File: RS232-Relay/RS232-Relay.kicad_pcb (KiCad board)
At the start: 2 copper layers, 82.5 x 151 mm, 133 parts, among them J10 Relay 1-4, J11 Relay 1-4, J2 Conn_01x02, J4 Conn_01x09, J5 Conn_01x09, J7 RS232_1, J8 RS232_2, J9 Relay 1-4, K1 G5V-1, K13 G5V-1, K14 G5V-1, K15 G5V-1, K2 G5V-1, K3 G5V-1, K4 G5V-1, K5 G5V-1, K6 G5V-1, K7 G5V-1, K8 G5V-1, K9 G5V-1, Q1 2N3904, Q13 2N3904, Q14 2N3904, Q15 2N3904, Q2 2N3904, Q3 2N3904, Q4 2N3904, Q5 2N3904, Q6 2N3904, Q7 2N3904, Q8 2N3904, Q9 2N3904, SW2 SW_SPST, SW3 SW_SPST, U1 TEC2-1210WI, U2 LTV-847S, U3 PCF8575DBR, U4 MAX3232, U5 LTV-847S, U6 LTV-847S

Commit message: Port labels
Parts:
- added G***: LOGO, LOGO, F.Cu at (142.4, 110.6)
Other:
- board text added: "01"
- board text added: "02"
- board text added: "03"
- board text added: "04"
- board text added: "05"
- board text added: "06"
- board text added: "07"
- board text added: "08"
- board text added: "09"
- board text added: "0V"
- board text added: "10"
- board text added: "11"
- board text added: "12"
- board text added: "12V"

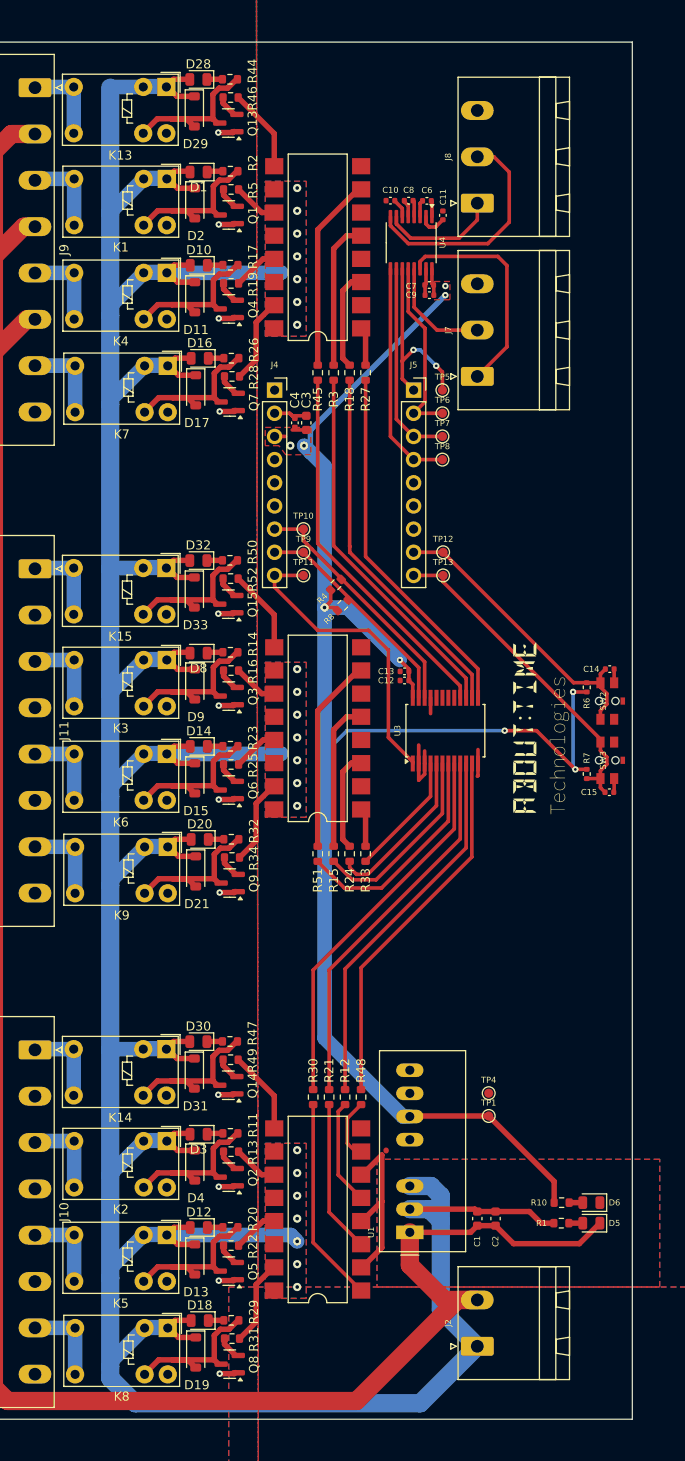
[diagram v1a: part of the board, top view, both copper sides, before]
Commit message: Hide silkscreen designators
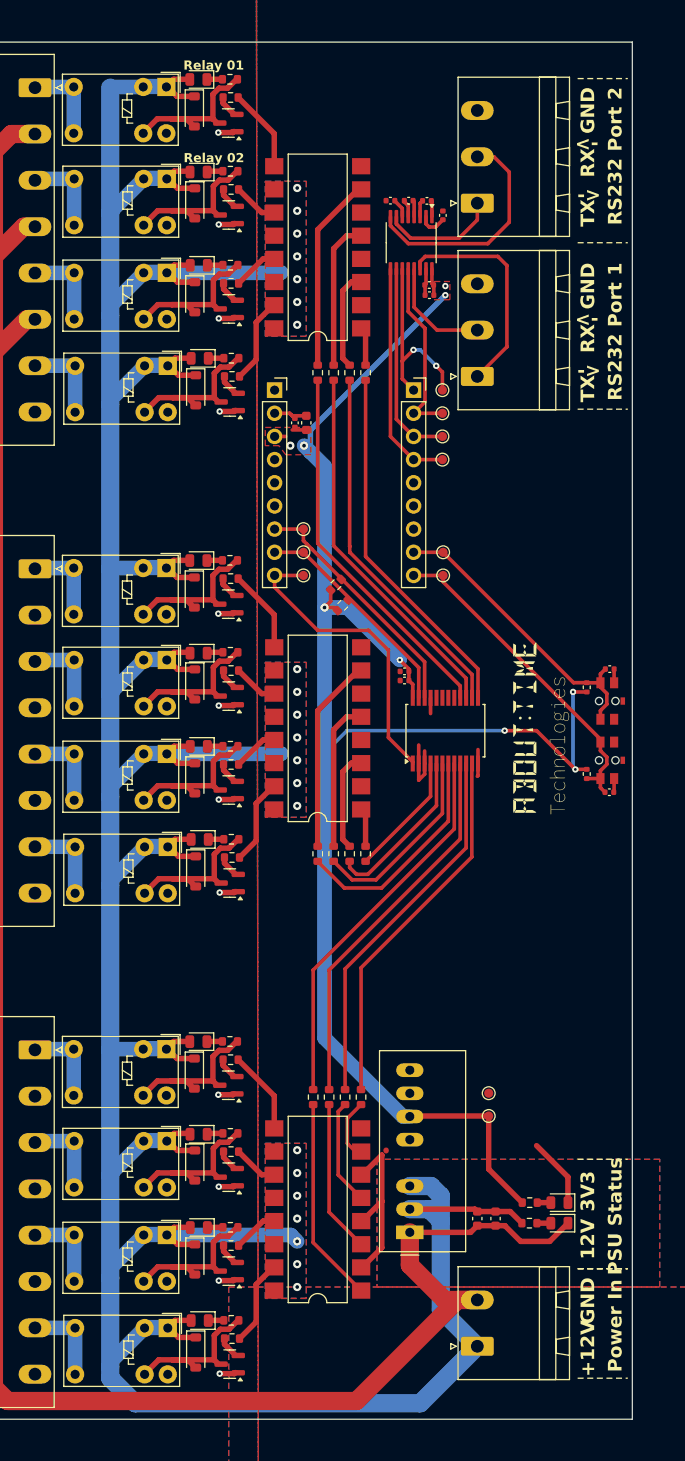
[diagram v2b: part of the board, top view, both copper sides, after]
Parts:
- moved D5 3.50 mm to (143.0, 165.0)
- moved D6 3.50 mm to (143.0, 162.8)
- moved R1 3.50 mm to (139.7, 165.0)
- moved R10 3.50 mm to (139.8, 162.8)
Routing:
- net GNDREF: track 41.8 -> 49.5 mm
- net GND: track 267.6 -> 263.9 mm
- net +12V: track 467.1 -> 463.6 mm
- net +3V3: track 191.4 -> 190.0 mm
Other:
- board text added: "+12V"
- board text added: "->"
- board text added: "3V3"
- board text added: "GND"
- board text added: "PSU Status"
- board text added: "Power In"
- board text added: "RS232 Port 1"
- board text added: "RS232 Port 2"
- board text added: "RX"
- board text added: "Relay 01"
- board text added: "Relay 02"
- board text added: "TX"

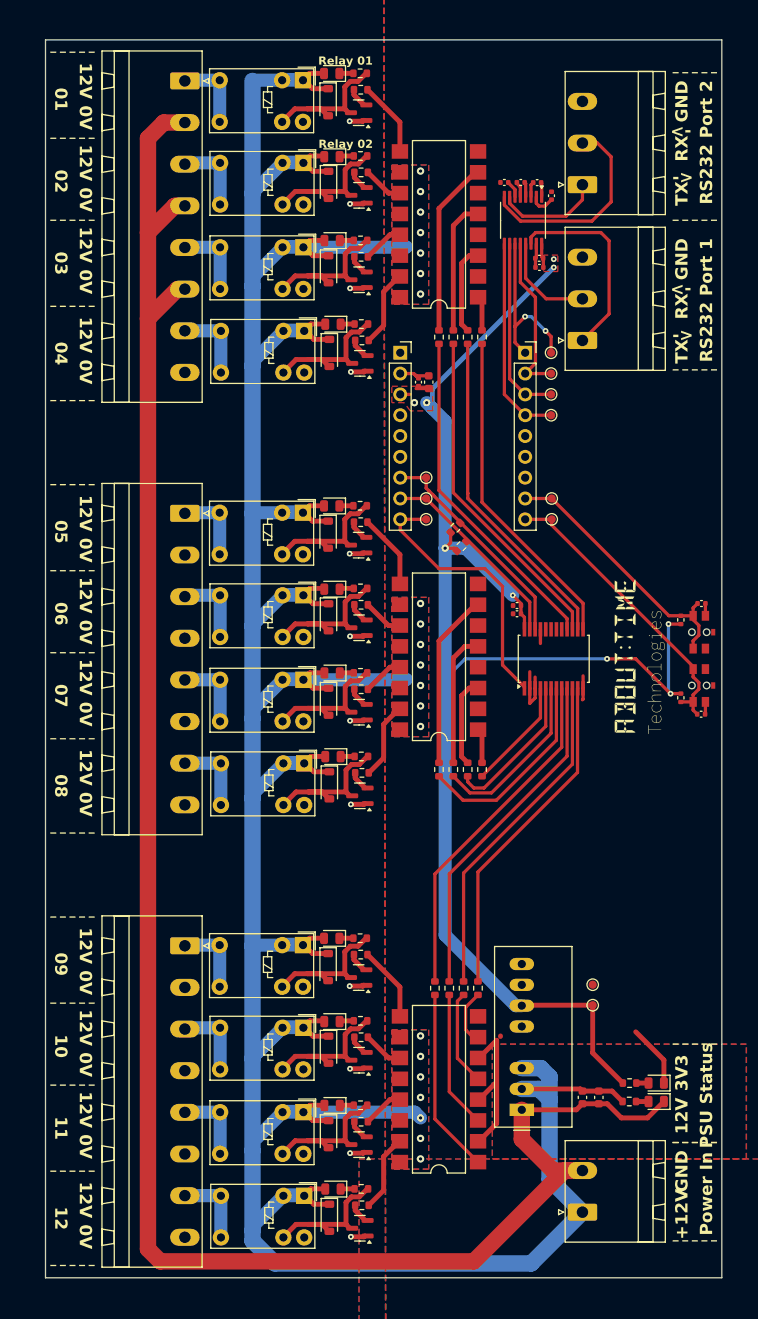
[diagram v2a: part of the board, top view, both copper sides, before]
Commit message: Silkscreen finished and vias added
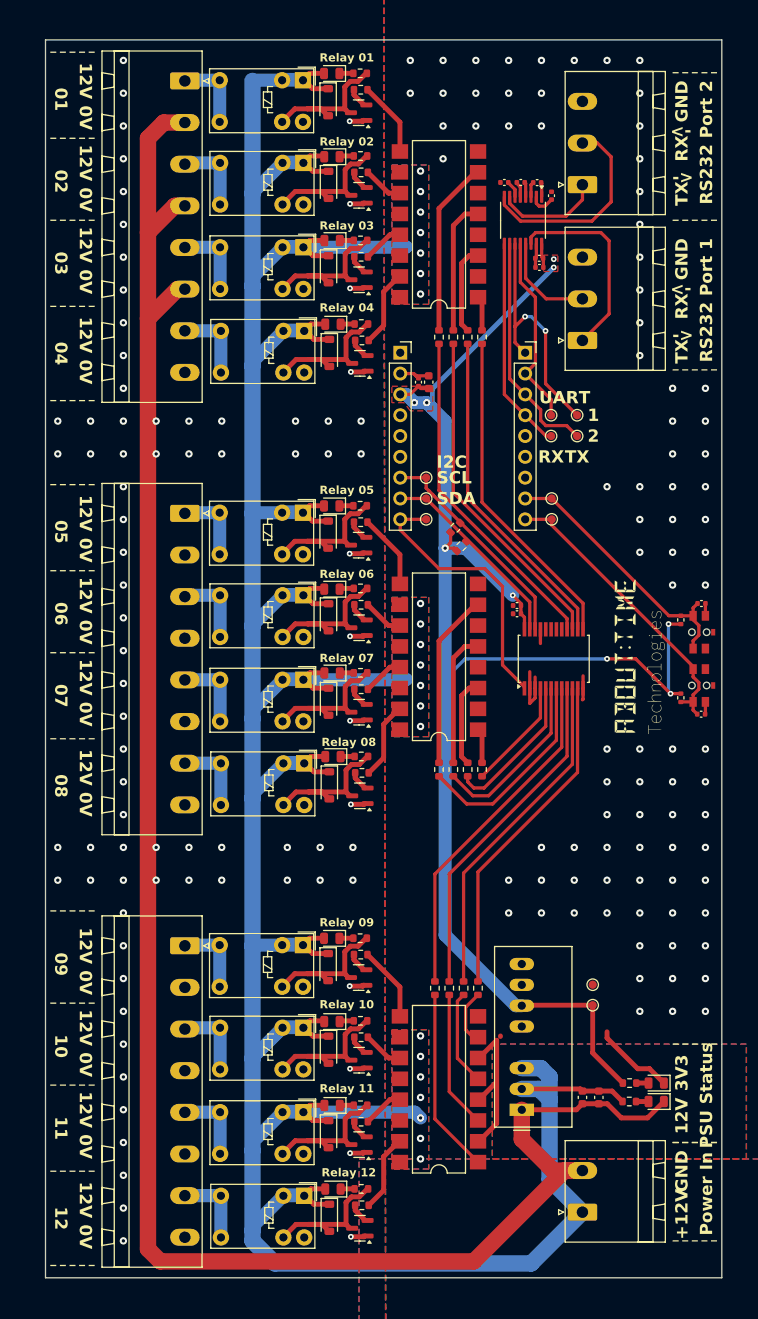
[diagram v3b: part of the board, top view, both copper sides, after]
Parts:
- moved TP5 8.25 mm to (133.3, 81.3)
- moved TP7 5.99 mm to (133.3, 83.8)
- moved TP6 5.08 mm to (130.2, 81.3)
- moved TP8 2.54 mm to (130.2, 83.8)
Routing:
- net UART_1_TX: track 21.7 -> 30.7 mm
- net UART_2_TX: track 22.3 -> 28.4 mm
- net +3V3: track 190.0 -> 194.9 mm
- net UART_1_RX: track 20.3 -> 23.5 mm
- net GNDREF: track 49.5 -> 51.8 mm, vias 0 -> 86
- net UART_2_RX: track 25.1 -> 26.2 mm
- net GND: vias 12 -> 81
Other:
- board text added: "1"
- board text added: "2"
- board text added: "I2C"
- board text added: "Relay 03"
- board text added: "Relay 04"
- board text added: "Relay 05"
- board text added: "Relay 06"
- board text added: "Relay 07"
- board text added: "Relay 08"
- board text added: "Relay 09"
- board text added: "Relay 10"
- board text added: "Relay 11"
- board text added: "Relay 12"
- board text added: "SCL"
- board text added: "SDA"
- board text added: "UART"

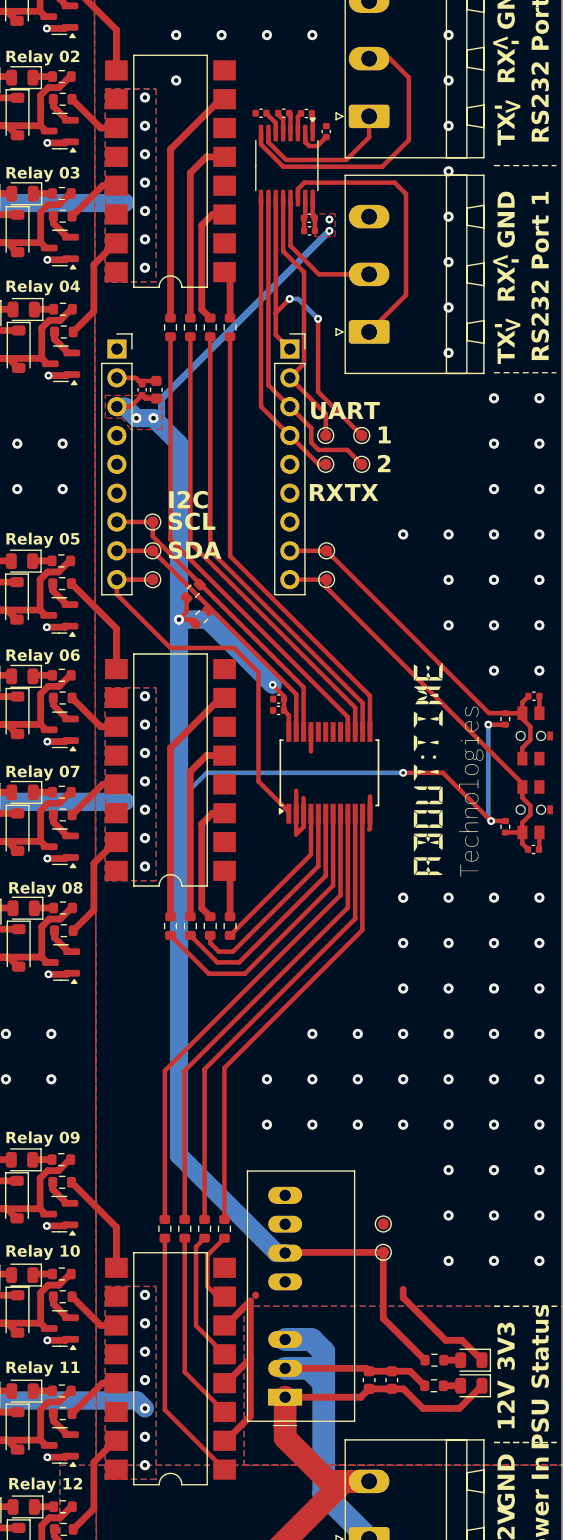
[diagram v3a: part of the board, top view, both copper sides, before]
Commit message: Switching to drain rather than source
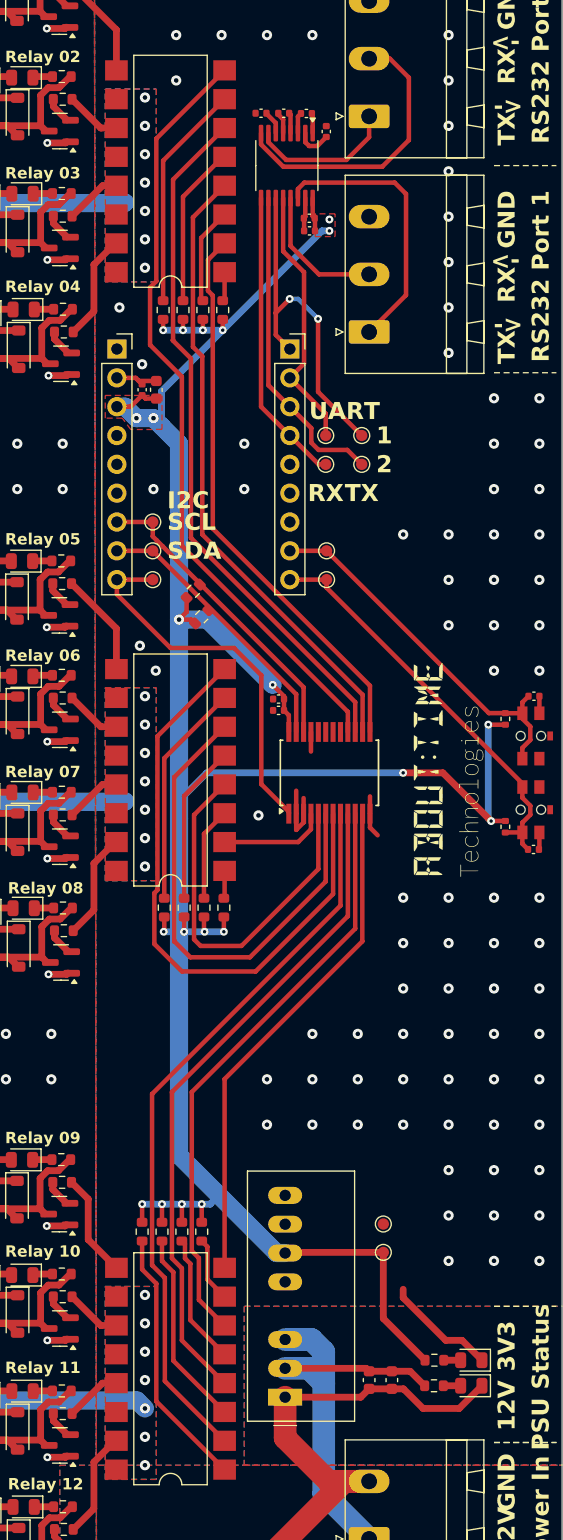
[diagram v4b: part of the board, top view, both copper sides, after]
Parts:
- moved R12 2.02 mm to (117.5, 151.4)
- moved R21 2.02 mm to (115.7, 151.4)
- moved R30 2.02 mm to (114.0, 151.4)
- moved R48 2.02 mm to (119.2, 151.4)
- moved R51 1.72 mm to (115.9, 122.9)
- moved R33 1.72 mm to (121.2, 122.9)
- moved R15 1.72 mm to (117.7, 122.9)
- moved R24 1.72 mm to (119.5, 122.9)
- moved R45 1.66 mm to (115.8, 70.2)
- moved R18 1.66 mm to (119.3, 70.2)
- moved R27 1.66 mm to (121.1, 70.2)
- moved R3 1.66 mm to (117.6, 70.2)
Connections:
- R12 pad 2: RELAY_IN_06 -> +3V3
- R15 pad 2: RELAY_IN_10 -> +3V3
- R18 pad 2: RELAY_IN_03 -> +3V3
- R21 pad 2: RELAY_IN_07 -> +3V3
- R24 pad 2: RELAY_IN_11 -> +3V3
- R27 pad 2: RELAY_IN_04 -> +3V3
- R3 pad 2: RELAY_IN_02 -> +3V3
- R30 pad 2: RELAY_IN_08 -> +3V3
- R33 pad 2: RELAY_IN_12 -> +3V3
- R45 pad 2: RELAY_IN_01 -> +3V3
- R48 pad 2: RELAY_IN_05 -> +3V3
- R51 pad 2: RELAY_IN_09 -> +3V3
- U2 pad 2: GNDREF -> RELAY_IN_04
- U2 pad 4: GNDREF -> RELAY_IN_03
- U2 pad 6: GNDREF -> RELAY_IN_02
- U2 pad 8: GNDREF -> RELAY_IN_01
- U5 pad 2: GNDREF -> RELAY_IN_08
- U5 pad 4: GNDREF -> RELAY_IN_07
- U5 pad 6: GNDREF -> RELAY_IN_06
- U5 pad 8: GNDREF -> RELAY_IN_05
- U6 pad 2: GNDREF -> RELAY_IN_12
- U6 pad 4: GNDREF -> RELAY_IN_11
- U6 pad 6: GNDREF -> RELAY_IN_10
- U6 pad 8: GNDREF -> RELAY_IN_09
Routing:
- net +3V3: track 194.9 -> 228.4 mm, vias 9 -> 21
- net RELAY_IN_09: track 25.3 -> 53.4 mm
- net RELAY_IN_01: track 41.3 -> 68.2 mm
- net RELAY_IN_08: track 42.2 -> 64.8 mm
- net RELAY_IN_10: track 21.5 -> 43.4 mm
- net RELAY_IN_02: track 40.8 -> 61.8 mm
- net GNDREF: track 51.8 -> 32.0 mm, vias 86 -> 94
- net RELAY_IN_07: track 41.7 -> 58.5 mm
- net RELAY_IN_11: track 18.3 -> 33.6 mm
- net RELAY_IN_03: track 40.4 -> 55.5 mm
- net RELAY_IN_06: track 41.2 -> 52.3 mm
- net RELAY_IN_04: track 39.9 -> 49.6 mm
- net RELAY_IN_05: track 40.8 -> 45.4 mm
- net RELAY_IN_12: track 13.7 -> 9.45 mm
- net /Relay-Module2/Relay-NO-ISO2/OPTO_LEFT_IN: track 10.9 -> 8.24 mm
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
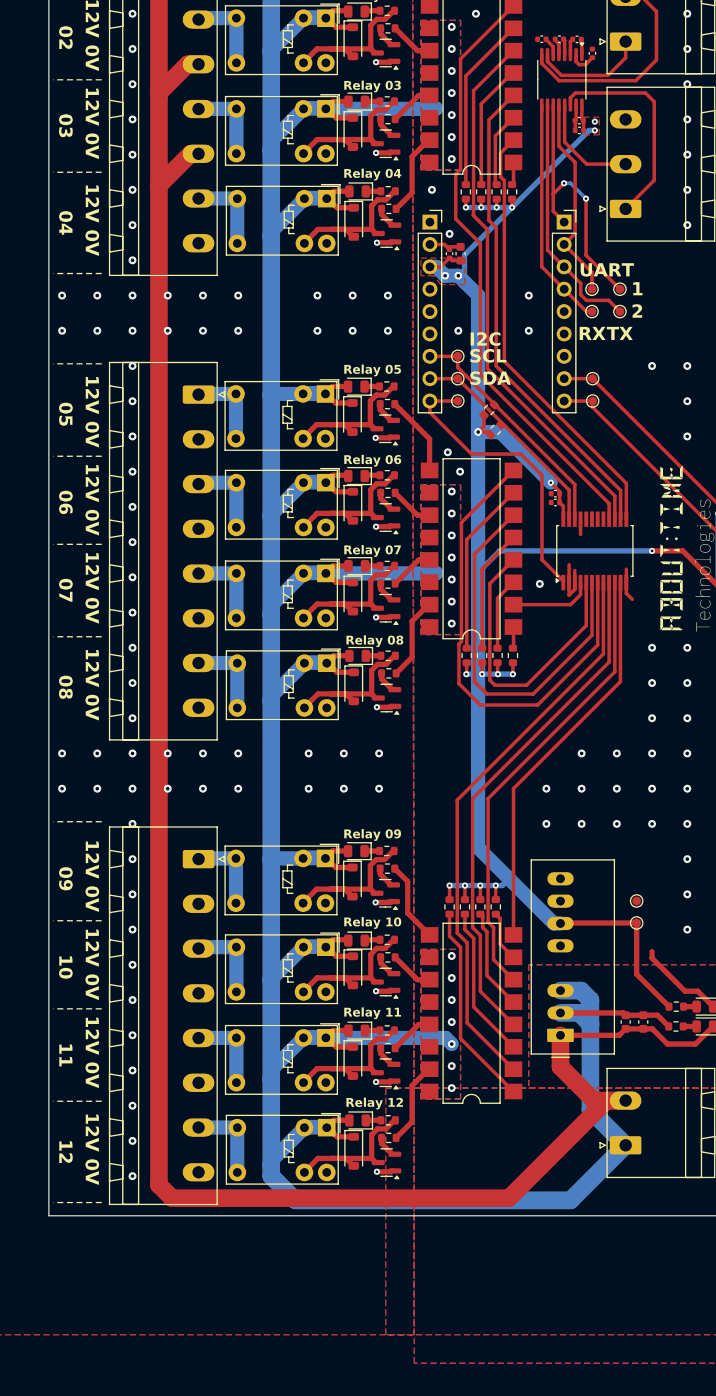
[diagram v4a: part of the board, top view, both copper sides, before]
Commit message: Figuring out the relay NC/NO connections
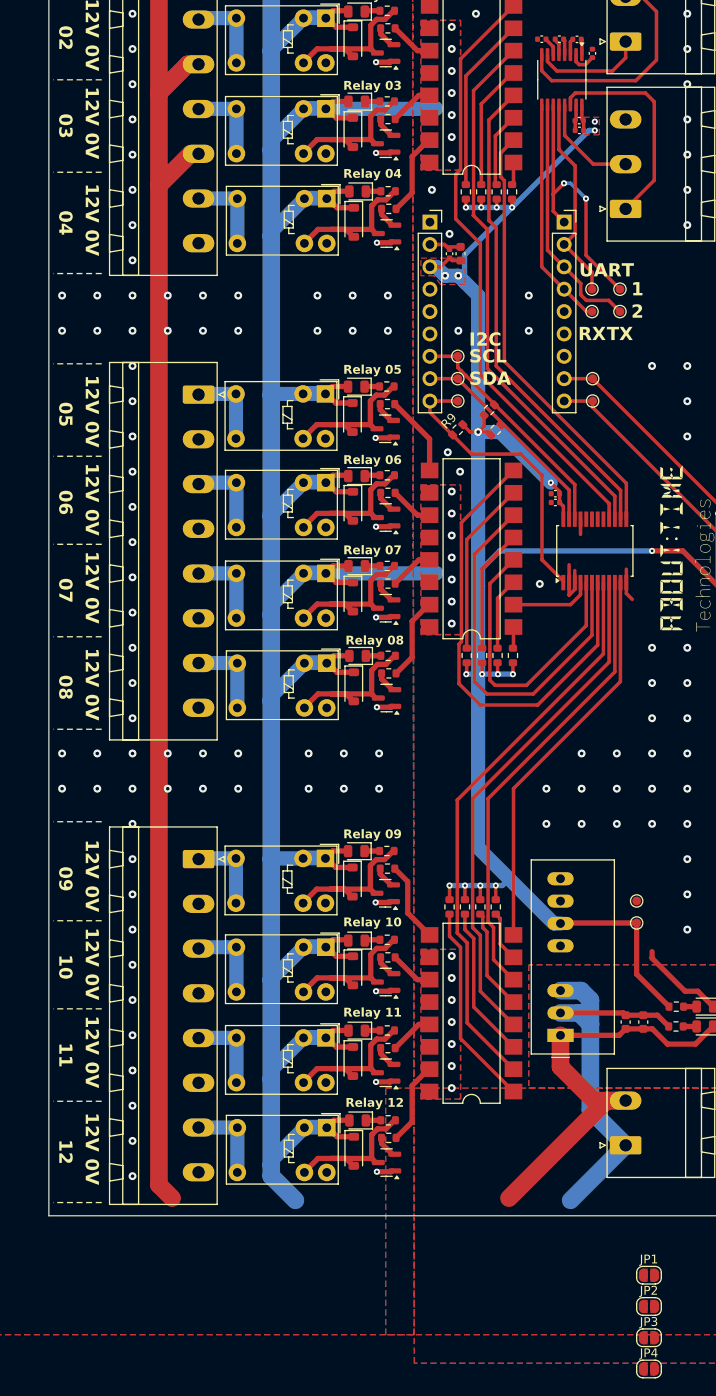
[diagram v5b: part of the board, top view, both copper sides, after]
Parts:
- added JP1: Jumper_2_Bridged, Jumper:SolderJumper-2_P1.3mm_Open_RoundedPad1.0x1.5mm, F.Cu at (136.7, 193.2)
- added JP2: Jumper_2_Open, Jumper:SolderJumper-2_P1.3mm_Open_RoundedPad1.0x1.5mm, F.Cu at (136.7, 196.8)
- added JP3: Jumper_2_Bridged, Jumper:SolderJumper-2_P1.3mm_Open_RoundedPad1.0x1.5mm, F.Cu at (136.7, 200.3)
- added JP4: Jumper_2_Open, Jumper:SolderJumper-2_P1.3mm_Open_RoundedPad1.0x1.5mm, F.Cu at (136.7, 203.9)
- added R9: 4K7, Resistor_SMD:R_0603_1608Metric, F.Cu at (114.9, 97.2)
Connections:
- D1 pad 2: +12V -> RELAY_ON
- D10 pad 2: +12V -> RELAY_ON
- D11 pad 1: +12V -> RELAY_ON
- D12 pad 2: +12V -> RELAY_ON
- D13 pad 1: +12V -> RELAY_ON
- D14 pad 2: +12V -> RELAY_ON
- D15 pad 1: +12V -> RELAY_ON
- D16 pad 2: +12V -> RELAY_ON
- D17 pad 1: +12V -> RELAY_ON
- D18 pad 2: +12V -> RELAY_ON
- D19 pad 1: +12V -> RELAY_ON
- D2 pad 1: +12V -> RELAY_ON
- D20 pad 2: +12V -> RELAY_ON
- D21 pad 1: +12V -> RELAY_ON
- D28 pad 2: +12V -> RELAY_ON
- D29 pad 1: +12V -> RELAY_ON
- D3 pad 2: +12V -> RELAY_ON
- D30 pad 2: +12V -> RELAY_ON
- D31 pad 1: +12V -> RELAY_ON
- D32 pad 2: +12V -> RELAY_ON
- D33 pad 1: +12V -> RELAY_ON
- D4 pad 1: +12V -> RELAY_ON
- D8 pad 2: +12V -> RELAY_ON
- D9 pad 1: +12V -> RELAY_ON
- K1 pad 1: +12V -> RELAY_ON
- K1 pad 10: GND -> RELAY_ON
- K1 pad 2: +12V -> RELAY_ON
- K13 pad 1: +12V -> RELAY_ON
- K13 pad 10: GND -> RELAY_ON
- K13 pad 2: +12V -> RELAY_ON
- K14 pad 1: +12V -> RELAY_ON
- K14 pad 10: GND -> RELAY_ON
- K14 pad 2: +12V -> RELAY_ON
- K15 pad 1: +12V -> RELAY_ON
- K15 pad 10: GND -> RELAY_ON
- K15 pad 2: +12V -> RELAY_ON
- K2 pad 1: +12V -> RELAY_ON
- K2 pad 10: GND -> RELAY_ON
- K2 pad 2: +12V -> RELAY_ON
- K3 pad 1: +12V -> RELAY_ON
- K3 pad 10: GND -> RELAY_ON
- K3 pad 2: +12V -> RELAY_ON
- K4 pad 1: +12V -> RELAY_ON
- K4 pad 10: GND -> RELAY_ON
- K4 pad 2: +12V -> RELAY_ON
- K5 pad 1: +12V -> RELAY_ON
- K5 pad 10: GND -> RELAY_ON
- K5 pad 2: +12V -> RELAY_ON
- K6 pad 1: +12V -> RELAY_ON
- K6 pad 10: GND -> RELAY_ON
- K6 pad 2: +12V -> RELAY_ON
- K7 pad 1: +12V -> RELAY_ON
- K7 pad 10: GND -> RELAY_ON
- K7 pad 2: +12V -> RELAY_ON
- K8 pad 1: +12V -> RELAY_ON
- K8 pad 10: GND -> RELAY_ON
- K8 pad 2: +12V -> RELAY_ON
- K9 pad 1: +12V -> RELAY_ON
- K9 pad 10: GND -> RELAY_ON
- K9 pad 2: +12V -> RELAY_ON
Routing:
- net +12V: track 463.6 -> 47.7 mm
- net RELAY_ON: track 0.00 -> 370.1 mm
- net GND: track 263.9 -> 225.7 mm
- net +3V3: track 228.4 -> 230.5 mm
